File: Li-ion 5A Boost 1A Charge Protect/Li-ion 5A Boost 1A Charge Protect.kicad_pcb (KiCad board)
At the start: 2 copper layers, 58 x 39 mm, 44 parts, among them J1 USB_C_FEMALE, SW1 SW_SPST, U1 AP9101CK6, U2 ECH8695R-TL-W, U3 MCP73833T, U4 PAM2423AECADJR

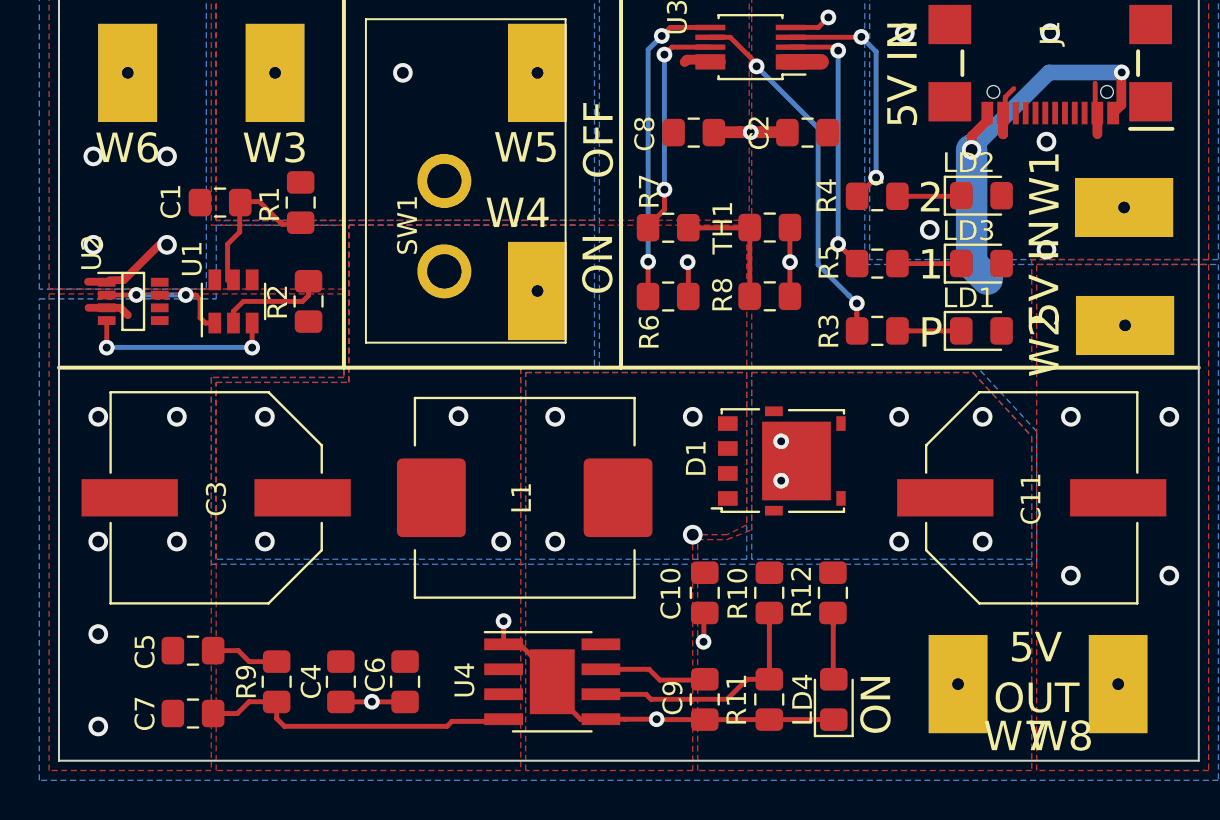
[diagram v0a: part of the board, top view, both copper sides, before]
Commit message: Standarizing libraries
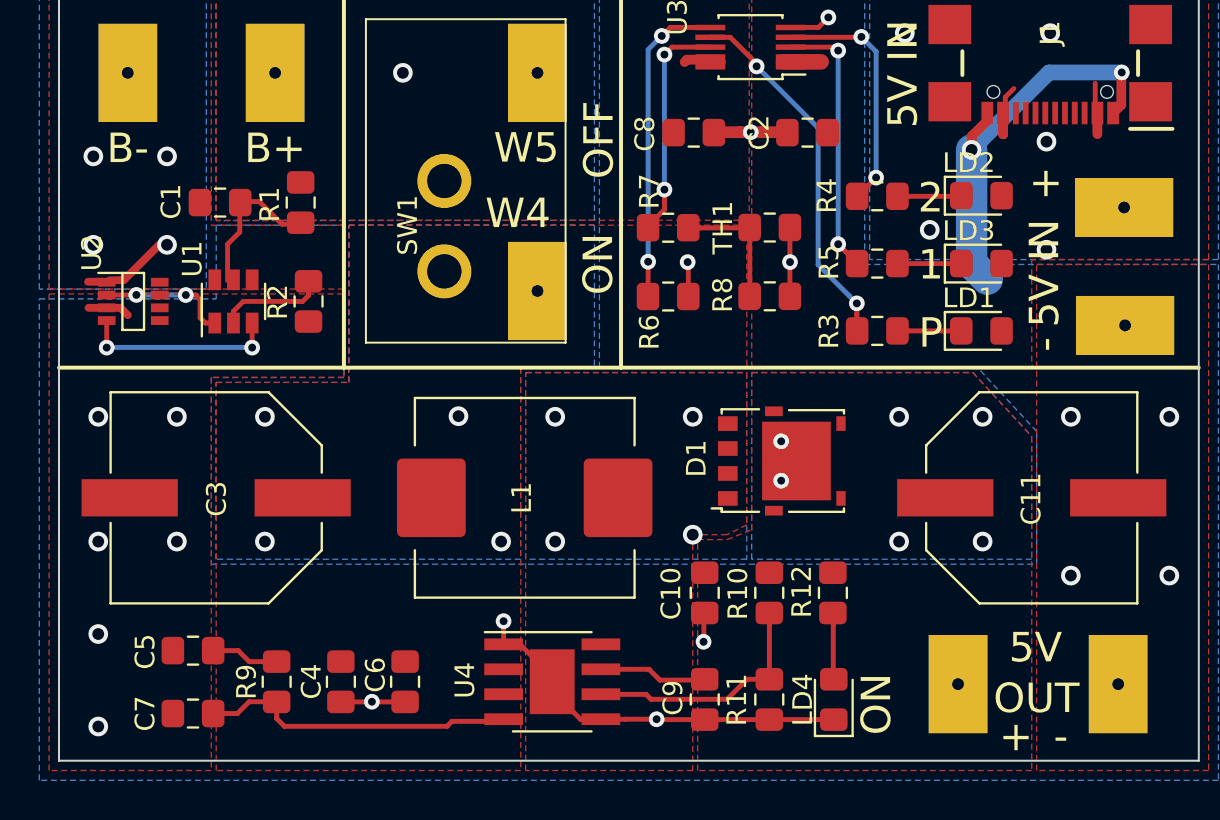
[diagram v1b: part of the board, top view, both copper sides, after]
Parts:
- removed W1: 2.5x5.0, Li-ion:Pad_3.0-5.0_w_TH
- added +: 2.5x5.0, Li-ion:Pad_3.0-5.0_w_TH, F.Cu at (170.2, 62.9)
- renumbered W7 to +, W8 to -, W2 to -, W3 to B+, W6 to B-
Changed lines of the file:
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@@
   (layers
     (0 Top signal)
-    (31 Bottom signal)
+    (31 Bottom signal hide)
     (32 B.Adhes user)
     (33 F.Adhes user)
     (34 B.Paste user)
     (35 F.Paste user)
-    (36 B.SilkS user)
+    (36 B.SilkS user hide)
     (37 F.SilkS user)
     (38 B.Mask user)
@@
     (solder_mask_min_width 0.25)
     (aux_axis_origin 0 0)
-    (visible_elements 7FFFFFFF)
+    (visible_elements 7FFEFFFF)
     (pcbplotparams
       (layerselection 0x010fc_ffffffff)
@@
     (add_net GND)
     (add_net "Net-(C5-Pad1)")
-    (add_net "Net-(J1-PadA5)")
-    (add_net "Net-(J1-PadA6)")
-    (add_net "Net-(J1-PadA7)")
-    (add_net "Net-(J1-PadA8)")
-    (add_net "Net-(J1-PadB5)")
-    (add_net "Net-(J1-PadB6)")
-    (add_net "Net-(J1-PadB7)")
-    (add_net "Net-(J1-PadB8)")
-    (add_net "Net-(J1-PadS1)")
-    (add_net "Net-(J1-PadS2)")
-    (add_net "Net-(J1-PadS3)")
-    (add_net "Net-(J1-PadS4)")
     (add_net "Net-(LD1-Pad1)")
     (add_net "Net-(LD2-Pad1)")
@@
     (add_net "Net-(U1-Pad1)")
     (add_net "Net-(U1-Pad3)")
-    (add_net "Net-(U1-Pad4)")
-    (add_net "Net-(U2-Pad5)")
-    (add_net "Net-(U2-Pad6)")
-    (add_net "Net-(U2-Pad7)")
-    (add_net "Net-(U2-Pad8)")
   )
   (net_class "High Power" ""
@@
     (at 169.9 87.105 180)
     (descr "SMD Pad 3.0x5.0 mm")
-    (fp_text reference W8 (at 2.92 -3.545 180) (layer F.SilkS)
+    (fp_text reference - (at 2.92 -3.545 180) (layer F.SilkS)
       (effects (font (size 1.5 1.5) (thickness 0.3)) (justify bottom))
     )
@@
     (at 161.75 87.105 180)
     (descr "SMD Pad 3.0x5.0 mm")
-    (fp_text reference W7 (at -2.95 -3.545 180) (layer F.SilkS)
+    (fp_text reference + (at -2.95 -3.545 180) (layer F.SilkS)
       (effects (font (size 1.5 1.5) (thickness 0.3)) (justify bottom))
     )
@@
     (at 119.5 56 180)
     (descr "SMD Pad 3.0x5.0 mm")
-    (fp_text reference W6 (at 0 -4.7225 180) (layer F.SilkS)
+    (fp_text reference B- (at 0 -4.7225 180) (layer F.SilkS)
       (effects (font (size 1.5 1.5) (thickness 0.3)) (justify bottom))
     )
@@
     (at 127 56)
     (descr "SMD Pad 3.0x5.0 mm")
-    (fp_text reference W3 (at 0 4.7225 180) (layer F.SilkS)
+    (fp_text reference B+ (at 0 4.7225 180) (layer F.SilkS)
       (effects (font (size 1.5 1.5) (thickness 0.3)) (justify bottom))
     )
@@
     (at 170.25 68.85 270)
     (descr "SMD Pad 3.0x5.0 mm")
-    (fp_text reference W2 (at 0.97 3.2 270) (layer F.SilkS)
+    (fp_text reference - (at 0.97 3.2 270) (layer F.SilkS)
       (effects (font (size 1.5 1.5) (thickness 0.3)) (justify bottom))
     )
@@
     (at 170.2 62.85 90)
     (descr "SMD Pad 3.0x5.0 mm")
-    (fp_text reference W1 (at 1.22 -3.15 270) (layer F.SilkS)
-      (effects (font (size 1.5 1.5) (thickness 0.3)) (justify bottom))
-    )
+    (fp_text reference + (at 1.22 -3.15 270) (layer F.SilkS)
+      (effects (font (size 1.5 1.5) (thickness 0.3)) (justify bottom))
+    )

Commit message: Library updates
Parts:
- added FID1: Fiducial, Fiducial_LE:Fiducial_1mm_Mask2mm, F.Cu at (180.6, 89.5)
- added FID2: Fiducial, Fiducial_LE:Fiducial_1mm_Mask2mm, F.Cu at (184.2, 89.5)
- added FID3: Fiducial, Fiducial_LE:Fiducial_1mm_Mask2mm, F.Cu at (187.7, 89.5)
- C1: value 100nF -> 0.1uF; footprint Li-ion:0805_2012Metric_HandSolder -> Frequently_Used_LE:0805_2012Metric_HandSolder
- C10, C2, C4, C5, C6, C7, C8, C9, R1, R10, R11, R12, R2, R3, R4, R5, R6, R7, R8, R9, TH1: footprint Li-ion:0805_2012Metric_HandSolder -> Frequently_Used_LE:0805_2012Metric_HandSolder
- C11, C3: footprint Li-ion:UCD1E471MNL1GS -> Li_Ion_LE:25TLV470M10X10.5
- D1: footprint Li-ion:NTS12120EMFST1G -> Li_Ion_LE:NTS12120EMFST1G
- J1: footprint Li-ion:GCT_USB4110-GF-A -> Connector_LE:GCT_USB4110-GF-A
- L1: footprint Li-ion:L_MGV1004 -> Li_Ion_LE:L_MGV1004
- LD1, LD2, LD3, LD4: footprint Li-ion:LED_0805_2012Metric_HandSolder -> Li_Ion_LE:LED_0805_2012Metric_HandSolder
- SW1: footprint Li-ion:GF1230054 -> Li_Ion_LE:GF1230054
- U1: footprint Li-ion:SOT-23-6 -> Li_Ion_LE:SOT-23-6
- U2: footprint Li-ion:SOT65P280X95-8N -> Li_Ion_LE:SOT65P280X95-8N
- U3: footprint Li-ion:MCP73833 -> Li_Ion_LE:MCP73833
- U4: footprint Li-ion:PAM2423AECADJR -> Li_Ion_LE:PAM2423AECADJR
- W1, W7: renamed from +; footprint Li-ion:Pad_3.0-5.0_w_TH -> Li_Ion_LE:Pad_3.0-5.0_w_TH
- W2, W8: renamed from -; footprint Li-ion:Pad_3.0-5.0_w_TH -> Li_Ion_LE:Pad_3.0-5.0_w_TH
- W3: renamed from W5; footprint Li-ion:Pad_3.0-5.0_w_TH -> Li_Ion_LE:Pad_3.0-5.0_w_TH
- W4: footprint Li-ion:Pad_3.0-5.0_w_TH -> Li_Ion_LE:Pad_3.0-5.0_w_TH
- W5: renamed from B+; footprint Li-ion:Pad_3.0-5.0_w_TH -> Li_Ion_LE:Pad_3.0-5.0_w_TH
- W6: renamed from B-; footprint Li-ion:Pad_3.0-5.0_w_TH -> Li_Ion_LE:Pad_3.0-5.0_w_TH
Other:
- board text added: "SW"

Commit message: Updates after first build, intermediate check in
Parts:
- added FID4: Fiducial, Fiducial_LE:Fiducial_1mm_Mask2mm, F.Cu at (185.2, 113.0)
- added H1: MountingHole, MountingHole:MountingHole_2.5mm_Pad, F.Cu at (103.8, 96.1)
- added H2: MountingHole, MountingHole:MountingHole_2.5mm_Pad, F.Cu at (141.9, 96.0)
- added H3: MountingHole, MountingHole:MountingHole_2.5mm_Pad, F.Cu at (205.2, 111.2)
- added H4: MountingHole, MountingHole:MountingHole_2.5mm_Pad, F.Cu at (195.2, 109.4)
- C1, C10, C2, C4, C5, C6, C7, C8, C9, R1, R10, R11, R12, R2, R3, R4, R5, R6, R7, R8, R9, TH1: footprint Frequently_Used_LE:0805_2012Metric_HandSolder -> Frequently_Used_LE:0603_1608Metric
- J1: footprint Connector_LE:GCT_USB4110-GF-A -> Connector_LE:GCT_USB4125-GF-A_REVA
- LD1, LD2, LD3, LD4: footprint Li_Ion_LE:LED_0805_2012Metric_HandSolder -> Frequently_Used_LE:LED_0805_2012Metric
- W1, W2, W3, W4, W5, W6, W7, W8: value 2.5x5.0 -> 2.0x3.25; footprint Li_Ion_LE:Pad_3.0-5.0_w_TH -> Li_Ion_LE:Pad_2.0-3.25_w_TH
- moved FID2 24.2 mm to (178.4, 113.0)
- moved FID3 24.2 mm to (181.9, 113.0)
- moved FID1 24.2 mm to (174.8, 113.0)
- moved W8 19.1 mm to (153.9, 97.6)
- moved U1 18.8 mm to (108.4, 76.6)
- moved U2 18.8 mm to (103.3, 76.6)
- moved R2 18.8 mm to (112.2, 76.6)
- moved J1 18.6 mm to (150.4, 66.4)
- moved R1 18.4 mm to (112.3, 71.6)
- moved C2 18.4 mm to (138.1, 68.0)
- moved C8 18.4 mm to (132.3, 68.0)
- moved TH1 18.4 mm to (136.2, 72.9)
- moved C10 18.4 mm to (132.9, 91.5)
- moved C3 18.4 mm to (108.0, 86.6)
- moved C4 18.4 mm to (114.3, 96.0)
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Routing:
- net GND: track 58.3 -> 47.9 mm
- net /VUSB: track 7.15 -> 2.10 mm, vias 5 -> 0
- net /BATT-: track 4.07 -> 1.52 mm
- net Net-(LD4-Pad2): track 3.42 -> 1.27 mm
- net /COMP: track 16.2 -> 15.1 mm
- net Net-(C5-Pad1): track 3.33 -> 2.25 mm
- net Net-(U1-Pad1): track 6.68 -> 6.14 mm
- removed copper zone on B.Cu, net /VUSB
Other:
- rule pad_to_mask_clearance: 0.051 -> 0.0508
- board text added: "5V OUT"
- board text removed: "5V"

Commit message: Version 1.1 updates
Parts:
- removed FID1, FID2, FID3: Fiducial, Fiducial_LE:Fiducial_1mm_Mask2mm
- added F1: Fiducial, Fiducial_LE:Fiducial_1mm_Mask2mm, F.Cu at (101.5, 95.0)
- added F2: Fiducial, Fiducial_LE:Fiducial_1mm_Mask2mm, F.Cu at (131.7, 91.3)
- added F3: Fiducial, Fiducial_LE:Fiducial_1mm_Mask2mm, F.Cu at (152.0, 55.5)
- added Q1: BUK6D30-40E, Li_Ion_LE:BUK6D3040EX, F.Cu at (87.0, 75.2)
- added R13: 330, Frequently_Used_LE:0603_1608Metric, F.Cu at (91.7, 74.0)
- added R14: 10k, Frequently_Used_LE:0603_1608Metric, F.Cu at (91.7, 76.5)
- C11, C3: footprint Li_Ion_LE:25TLV470M10X10.5 -> Li_Ion_LE:CP_Elec_10x10.5
- H1, H2, H3, H4: footprint MountingHole:MountingHole_2.5mm_Pad -> MountingHole:MountingHole_2.2mm_M2
- J1: footprint Connector_LE:GCT_USB4125-GF-A_REVA -> Connector_LE:GCT_USB4110-GF-A
- SW1: footprint Li_Ion_LE:GF1230054 -> Button_Switch_LE:CL-SB-22A_Edge
- moved H4 104.2 mm to (106.0, 55.5)
- moved F4 102.2 mm to (101.0, 55.0)
- moved H3 82.5 mm to (143.0, 57.0)
- moved SW1 30.0 mm to (90.9, 66.8), turned to 270 degrees
- moved W4 25.3 mm to (117.6, 51.7)
- moved W3 14.5 mm to (124.7, 50.5)
- moved R12 13.4 mm to (136.2, 97.2), turned to 90 degrees
- moved LD4 13.3 mm to (139.3, 97.2), turned to 90 degrees
- moved H2 8.20 mm to (134.7, 92.2)
- moved W8 7.90 mm to (146.0, 97.4)
- moved R11 6.57 mm to (129.6, 97.2)
- moved C10 6.52 mm to (132.5, 98.0), turned to 180 degrees
- moved R10 6.14 mm to (132.5, 96.4), turned to 180 degrees
- moved C11 5.88 mm to (144.3, 88.2)
- moved C9 5.49 mm to (127.4, 97.2)
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- renumbered FID4 to F4
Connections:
- C10 pad 2: GND -> /BGND
- C11 pad 2: GND -> /BGND
- C3 pad 1: /BOOSTVIN -> /BATT+
- C3 pad 2: GND -> /BGND
- C4 pad 1: /BOOSTVIN -> /BATT+
- C4 pad 2: GND -> /BGND
- C5 pad 2: GND -> /BGND
- C6 pad 1: /BOOSTVIN -> /BATT+
- C6 pad 2: GND -> /BGND
- C7 pad 2: GND -> /BGND
- C9 pad 2: GND -> /BGND
- J1 pad A5: (no net) -> Net-(J1-PadA5)
- J1 pad B5: (no net) -> Net-(J1-PadB5)
- J1 pad S1: (no net) -> Net-(J1-PadS1)
- J1 pad S2: (no net) -> Net-(J1-PadS2)
- J1 pad S3: (no net) -> Net-(J1-PadS3)
- J1 pad S4: (no net) -> Net-(J1-PadS4)
- L1 pad 1: /BOOSTVIN -> /BATT+
- LD4 pad 1: GND -> /BGND
- R11 pad 2: GND -> /BGND
- SW1 pad 1: /BOOSTVIN -> Net-(R13-Pad2)
- U1 pad 4: (no net) -> Net-(U1-Pad4)
- U2 pad 5: (no net) -> Net-(U2-Pad5)
- U2 pad 6: (no net) -> Net-(U2-Pad6)
- U2 pad 7: (no net) -> Net-(U2-Pad7)
- U2 pad 8: (no net) -> Net-(U2-Pad8)
- U4 pad 1: GND -> /BGND
- U4 pad 2: /BOOSTVIN -> /BATT+
- U4 pad 3: /BOOSTVIN -> /BATT+
- U4 pad 5: GND -> /BGND
- U4 pad 9: GND -> /BGND
- W4 pad 1: /BOOSTVIN -> Net-(R13-Pad2)
- W8 pad 1: GND -> /BGND
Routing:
- net /BGND: track 0.00 -> 26.8 mm, vias 0 -> 12
- net GND: track 47.9 -> 22.9 mm, vias 20 -> 6
- net /FB: track 12.2 -> 7.73 mm
- net /COMP: track 15.1 -> 11.1 mm
- net /SS: track 5.48 -> 3.27 mm
- net Net-(LD4-Pad2): track 1.27 -> 3.22 mm
- net /BOOSTVOUT: vias 6 -> 4
- net /BOOSTVIN: vias 4 -> 0
- net /BATT+: vias 1 -> 5
- added copper zone on B.Cu, net /BGND
- added copper zone on F.Cu, net /BGND
- added copper zone on B.Cu, net Net-(R13-Pad2)
- removed copper zone on B.Cu, net /BOOSTVIN
- removed copper zone on F.Cu, net /BOOSTVIN
- removed copper zone on B.Cu, net GND
- removed copper zone on F.Cu, net GND
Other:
- board size 58 x 39 mm -> 51.5 x 39 mm
- board text added: "5V"
- board text removed: "5V OUT"

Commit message: Version 1.1 updates
Version 1.1 updates
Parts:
- SW1: value SW_SPST -> SW_DPST
- W3, W4: value 2.0x3.25 -> 1.5x2.5; footprint Li_Ion_LE:Pad_2.0-3.25_w_TH -> Li_Ion_LE:Pad_1.5-2.5_w_TH
- moved W3 36.0 mm to (101.5, 78.0), turned to 270 degrees
- moved W4 28.9 mm to (101.5, 75.6), turned to 90 degrees
- moved R2 26.0 mm to (132.3, 60.1), turned to 0 degrees
- moved U1 25.5 mm to (128.6, 61.0)
- moved C1 24.5 mm to (128.7, 58.1)
- moved R1 24.1 mm to (132.3, 58.1), turned to 0 degrees
- moved F3 23.6 mm to (136.4, 73.2)
- moved Q1 21.1 mm to (107.5, 80.2), turned to 90 degrees
- moved H4 20.8 mm to (106.8, 76.2)
- moved H3 15.6 mm to (135.1, 70.5)
- moved W1 15.4 mm to (138.8, 70.2), turned to 180 degrees
- moved W2 14.4 mm to (142.0, 70.2), turned to 0 degrees
- moved SW1 14.1 mm to (104.5, 70.6), turned to 180 degrees
- moved R14 12.8 mm to (103.8, 80.5), turned to 270 degrees
- moved R13 12.2 mm to (102.0, 80.5), turned to 270 degrees
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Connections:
- SW1 pad 1: Net-(R13-Pad2) -> Net-(SW1-Pad1)
- SW1 pad 3: (no net) -> Net-(R13-Pad2)
- SW1 pad 4: (no net) -> Net-(SW1-Pad1)
- SW1 pad 5: (no net) -> /BATT+
- SW1 pad 6: (no net) -> Net-(R13-Pad2)
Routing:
- net /PG: track 18.6 -> 4.30 mm
- net /PROG: track 16.2 -> 2.65 mm, vias 2 -> 1
- net /ST1: track 13.8 -> 3.90 mm
- net Net-(U1-Pad3): track 9.63 -> 0.00 mm, vias 2 -> 0
- net /ST2: track 12.4 -> 2.83 mm, vias 2 -> 1
- net /THRMIC: track 11.3 -> 2.22 mm, vias 2 -> 1
- net GND: track 22.9 -> 13.8 mm, vias 6 -> 7
- net /PVDD: track 7.78 -> 0.00 mm
- net /THRM: track 6.42 -> 0.00 mm
- net Net-(U1-Pad1): track 6.14 -> 0.00 mm, vias 2 -> 0
- net /PVM: track 5.08 -> 0.00 mm
- net /FB: track 7.73 -> 10.8 mm, vias 0 -> 2
- net /BGND: track 26.8 -> 24.3 mm, vias 12 -> 13
- net /VUSB: track 2.10 -> 4.57 mm
- net /COMP: track 11.1 -> 11.5 mm, vias 0 -> 2
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- added copper zone on B.Cu, net GND
- added copper zone on F.Cu, net GND
- removed copper zone on B.Cu, net /BATT+
- removed copper zone on B.Cu, net Net-(R13-Pad2)
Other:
- board size 51.5 x 39 mm -> 51.5 x 32 mm
- board text added: "ESW"
- board text added: "Li-Ion 5V 5.5A Output 1A Charge"
- board text added: "V1.1.0"
- board text removed: "IN"
- board text removed: "Li-Ion 5V 5A Output 1A Charge"
- board text removed: "OFF"
- board text removed: "SW"
- board text removed: "V1.0.0"

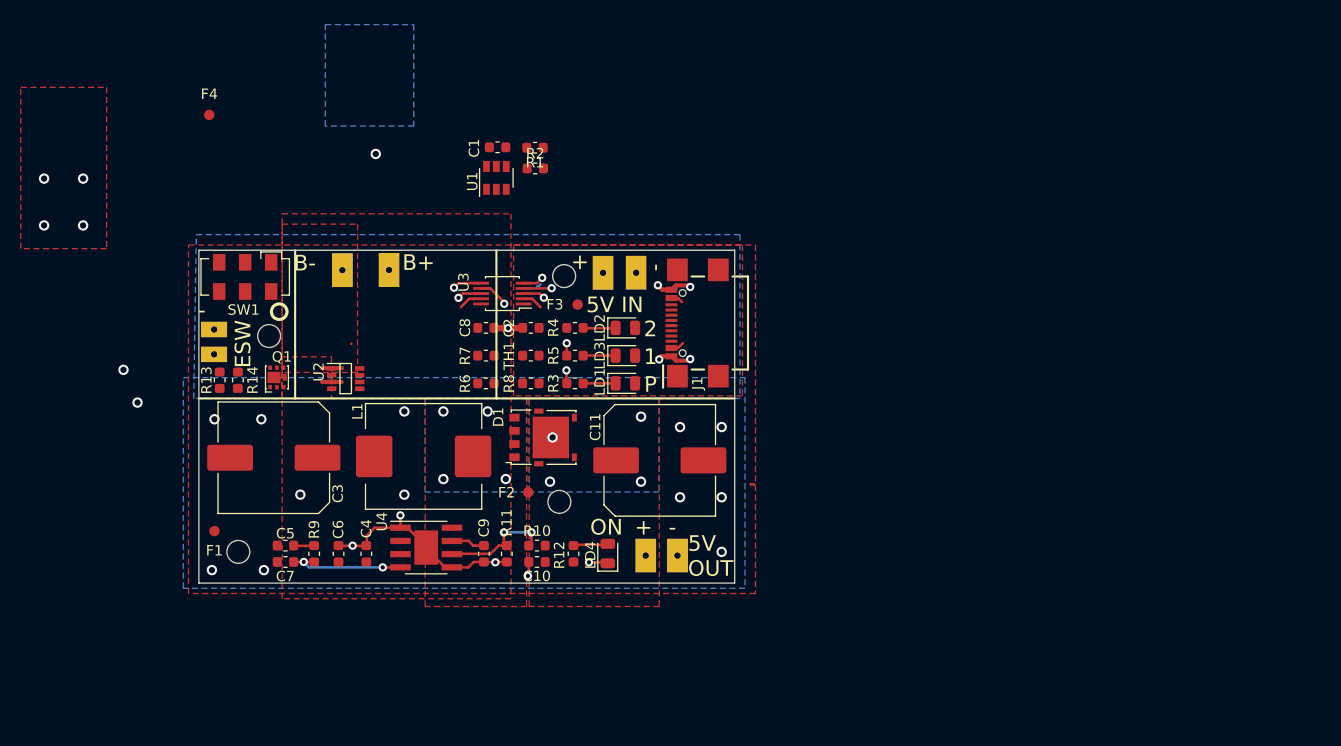
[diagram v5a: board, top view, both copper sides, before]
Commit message: Before moving protection IC
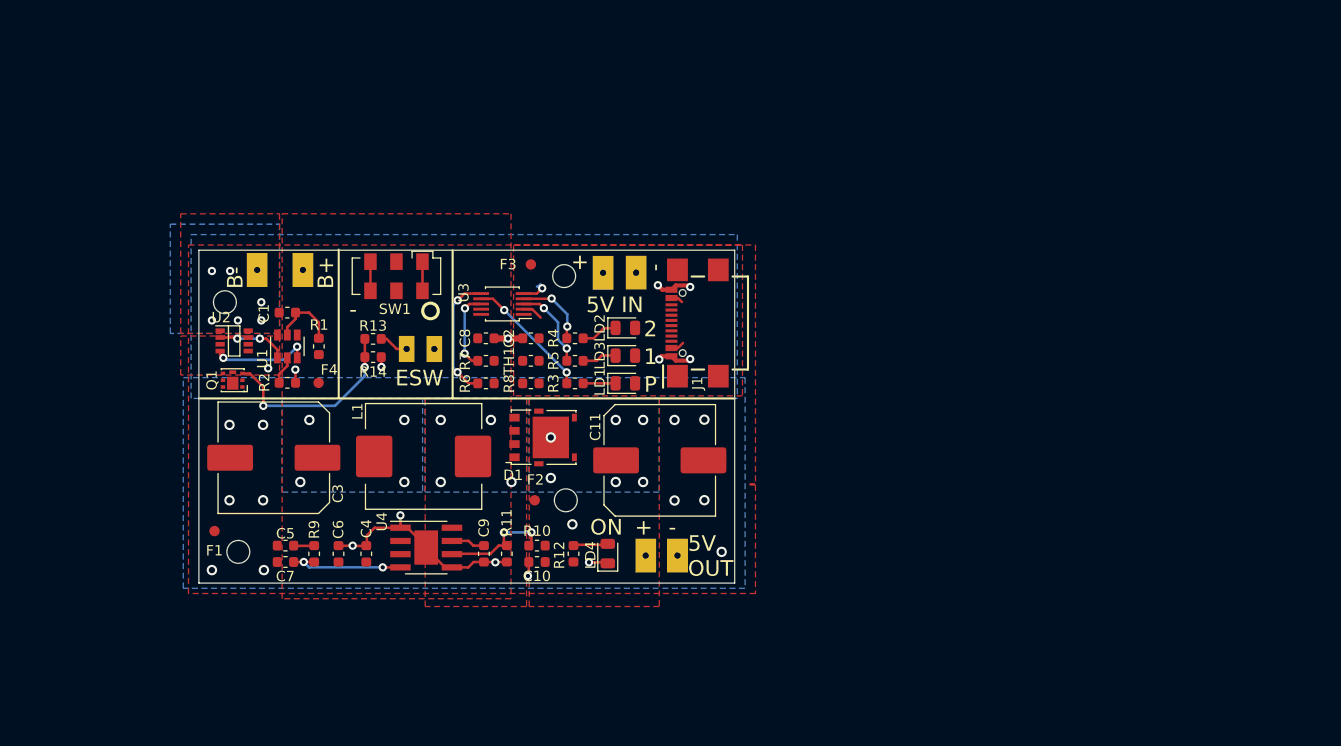
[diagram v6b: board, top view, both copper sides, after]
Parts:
- moved R2 31.5 mm to (108.5, 80.8)
- moved R1 28.2 mm to (111.5, 77.2), turned to 270 degrees
- moved F4 27.8 mm to (111.5, 80.8)
- moved U1 25.8 mm to (108.5, 77.2)
- moved C1 25.7 mm to (108.5, 74.0)
- moved W3 21.2 mm to (122.6, 77.5), turned to 180 degrees
- moved W4 18.6 mm to (120.0, 77.5), turned to 0 degrees
- moved R13 15.3 mm to (116.7, 76.5), turned to 0 degrees
- moved SW1 14.5 mm to (119.0, 70.5)
- moved R14 13.2 mm to (116.7, 78.3), turned to 180 degrees
- moved U2 11.3 mm to (103.4, 76.7)
- moved W5 8.28 mm to (110.0, 69.9)
- moved W6 8.19 mm to (105.6, 69.9)
- moved F3 5.93 mm to (131.9, 69.4)
- moved H4 5.35 mm to (102.5, 73.0)
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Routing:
- net Net-(Q1-Pad3): track 0.00 -> 18.9 mm, vias 0 -> 2
- net Net-(U1-Pad3): track 0.00 -> 9.55 mm, vias 0 -> 2
- net /PROG: track 2.65 -> 12.0 mm, vias 1 -> 2
- net /PG: track 4.30 -> 12.3 mm
- net Net-(U1-Pad1): track 0.00 -> 6.78 mm, vias 0 -> 2
- net /PVDD: track 0.00 -> 6.62 mm
- net Net-(R13-Pad2): track 0.00 -> 5.64 mm
- net /THRMIC: track 2.22 -> 7.51 mm, vias 1 -> 2
- net /ST2: track 2.83 -> 7.29 mm, vias 1 -> 2
- net /ST1: track 3.90 -> 8.26 mm
- net Net-(SW1-Pad1): track 0.00 -> 2.80 mm
- net /PVM: track 0.00 -> 2.73 mm
- net /BATT+: track 2.16 -> 0.00 mm, vias 5 -> 4
- net /BATT-: track 1.95 -> 0.00 mm, vias 4 -> 6
- net GND: track 13.8 -> 14.6 mm, vias 7 -> 9
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- added copper zone on B.Cu, net /BATT+

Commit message: Before reversing mosfet and protection IC
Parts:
- moved SW1 1.17 mm to (120.2, 70.5)
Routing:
- net /THRM: track 0.00 -> 4.91 mm
- net GND: track 14.6 -> 17.8 mm, vias 9 -> 11
- net /BATT+: track 0.00 -> 3.11 mm
- net /VUSB: track 4.57 -> 5.97 mm
- net /THRMIC: track 7.51 -> 8.39 mm
- net /SW: vias 4 -> 6
